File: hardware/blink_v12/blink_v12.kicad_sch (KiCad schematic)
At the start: 178 parts, among them J1 Conn_01x02, J14 Conn_02x16_Odd_Even, J15 Conn_01x01, J16 Conn_01x01, J5 Conn_01x06_Pin, J6 Conn_01x03, J7 Conn_01x06_Pin, J9 USB_C_Receptacle, Q1 AO3400A, Q2 AO3400A, Q3 2N7002, Q4 2N7002, Q5 2N7002, SW1 SW_SPDT, SW2 SW_Push_4PDT, SW3 SW_Push_4PDT, SW4 SW_Push_4PDT, U1 AMS1117-3.3, U10 TMP112AIDRLR, U11 MAX40200AUK, U12 MAX40200AUK, U13 AMS1117-3.3, U14 SN74LVC1G14DBV, U15 BQ29702DSER, U16 TPS63060, U3 M24C02-RMN, U4 STM32F405RGTx, U5 SN74LVC1G14DBV, U6 SN74LVC1G14DBV, U7 CH340C, U8 USBLC6-2P6, U9 MCP73832-2-OT, X1 GTXO-14V (2.048MHz), Y1 16MHz

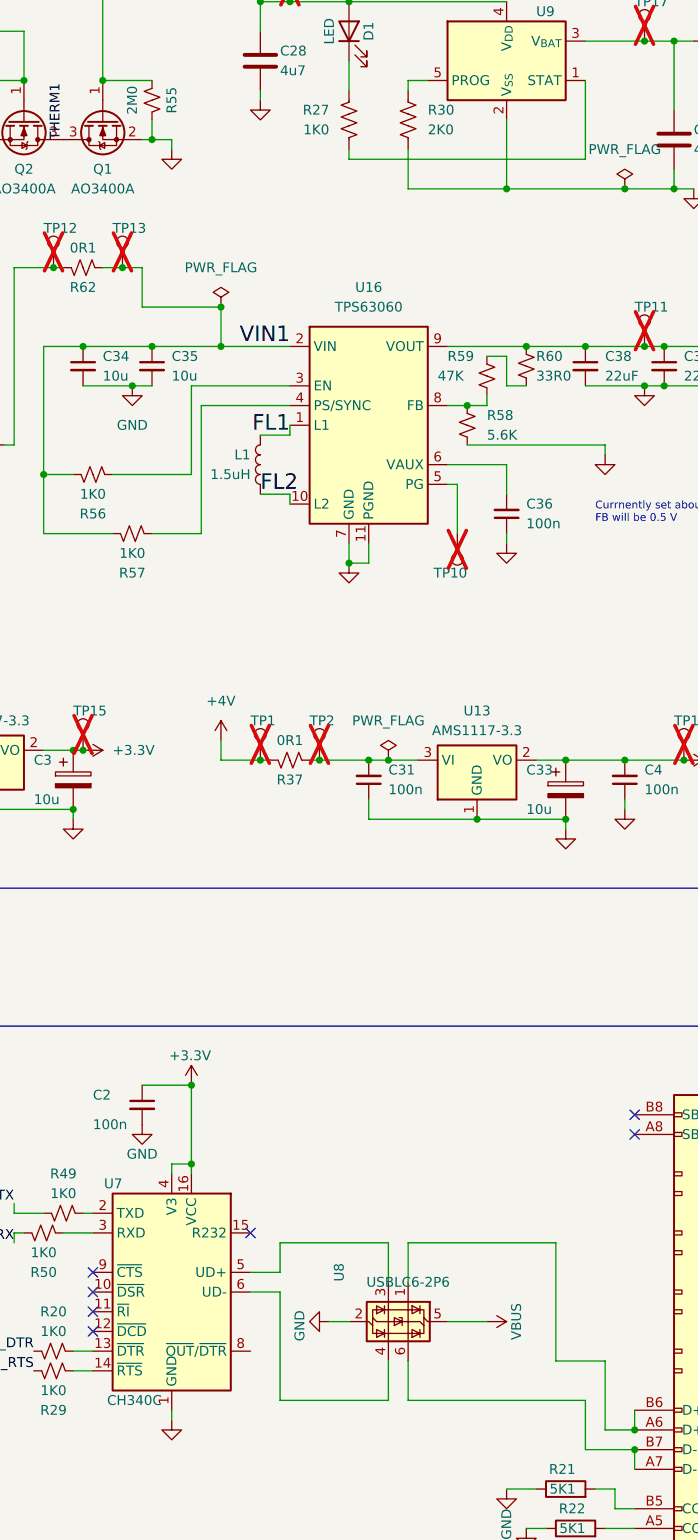
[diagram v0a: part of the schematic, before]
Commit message: fix symbol for USBLC6-2P6 that seems chaged in kicad 8
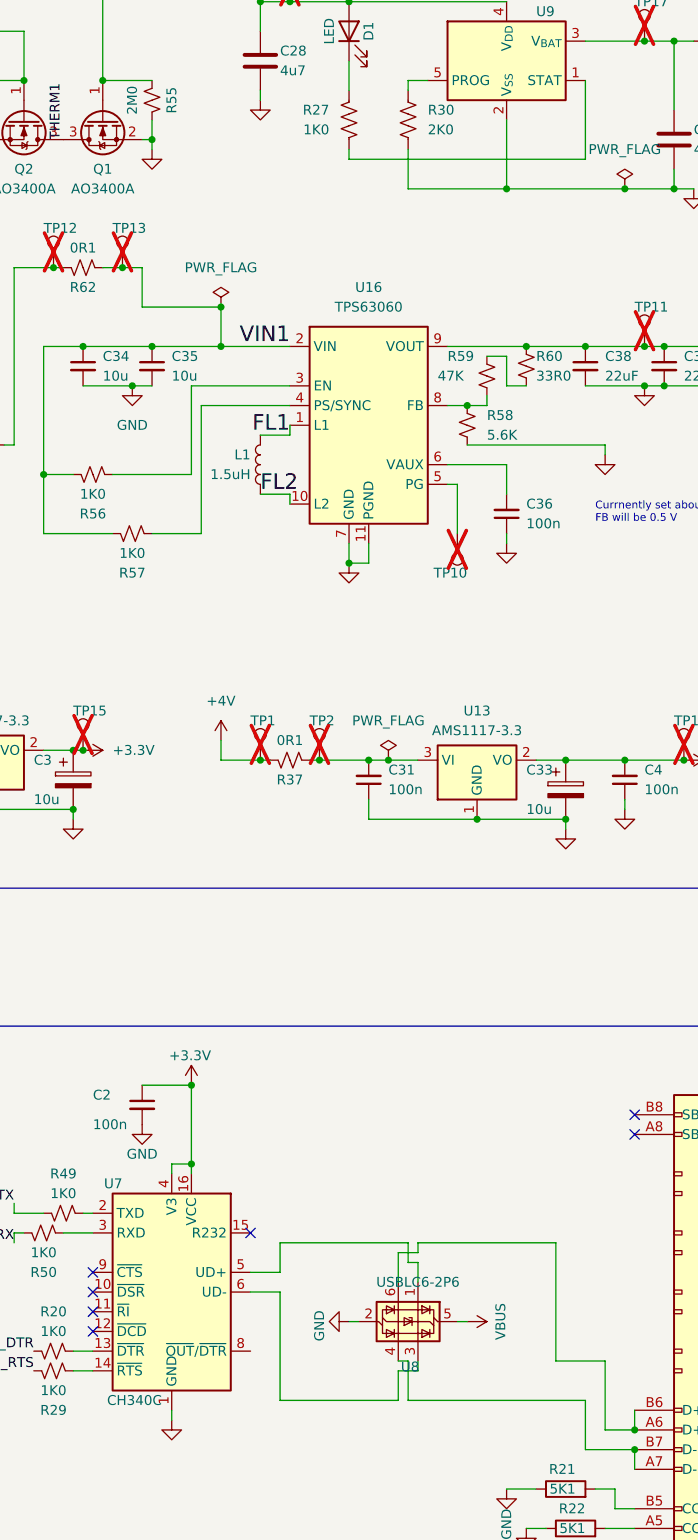
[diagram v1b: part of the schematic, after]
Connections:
- net at U7.5 (UD+): now also U8.1 (I/O1); no longer U8.3 (I/O2)
- net at U7.6 (UD-): now also U8.3 (I/O1); no longer U8.4 (I/O2)
- net at J9.A6 (D+), J9.B6 (D+): now also U8.6 (I/O2); no longer U8.1 (I/O1)
- net at J9.A7 (D-), J9.B7 (D-): now also U8.4 (I/O2); no longer U8.6 (I/O1)
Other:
- moved on the sheet: U8

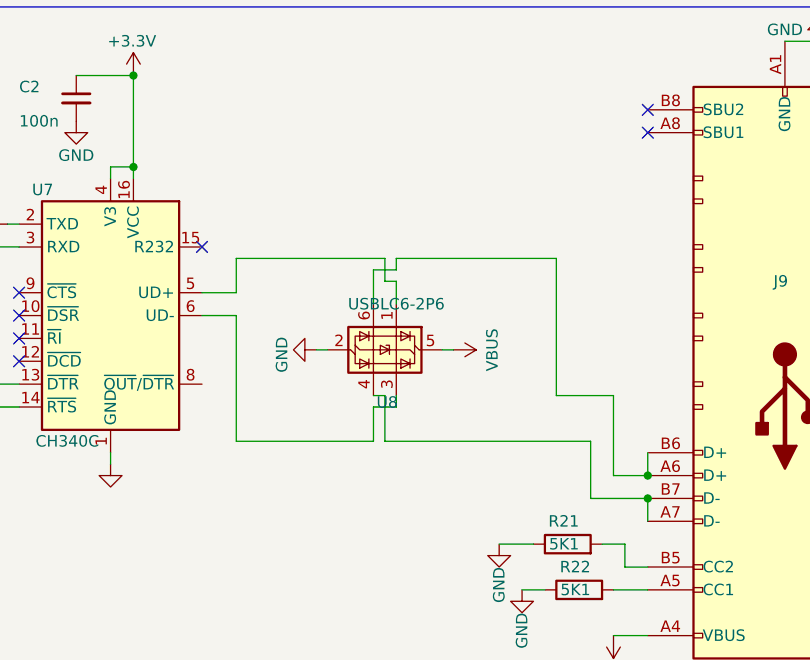
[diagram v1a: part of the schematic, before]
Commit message: fix up schematic for new USBLC6-2P6  footprint
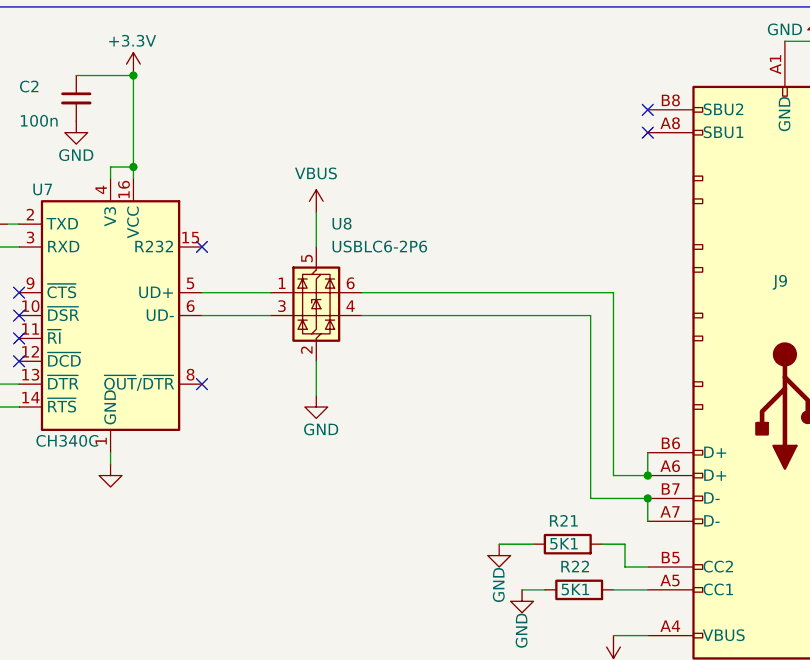
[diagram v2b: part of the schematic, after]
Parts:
- U8: JLCPCB Part # C2827693 -> (none); JLCPCB Rotation Offset 270 -> (none)
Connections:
- no-connect marks 42 -> 43

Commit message: remove the battery protection circuit
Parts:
- removed C37: 100n, Capacitor_SMD:C_0402_1005Metric, symbol Device:C_Small
- removed Q1, Q2: AO3400A, Package_TO_SOT_SMD:SOT-23, symbol Transistor_FET:AO3400A
- removed R14: 330R, Resistor_SMD:R_0603_1608Metric, symbol Device:R_Small_US
- removed R18: 2K2, Resistor_SMD:R_0603_1608Metric, symbol Device:R_Small_US
- removed R34, R55: 2M0, Resistor_SMD:R_0603_1608Metric, symbol Device:R_Small_US
- removed U15: BQ29702DSER, Package_SON:WSON-6_1.5x1.5mm_P0.5mm, symbol Battery_Management:BQ297xy
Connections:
- net GND: now also J1.1 (Pin_1), TP21.1

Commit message: moved the test points off rails
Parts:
- removed TP21, TP6, TP7, TP8: ~, TestPoint:TestPoint_THTPad_D1.5mm_Drill0.7mm, symbol Connector:TestPoint

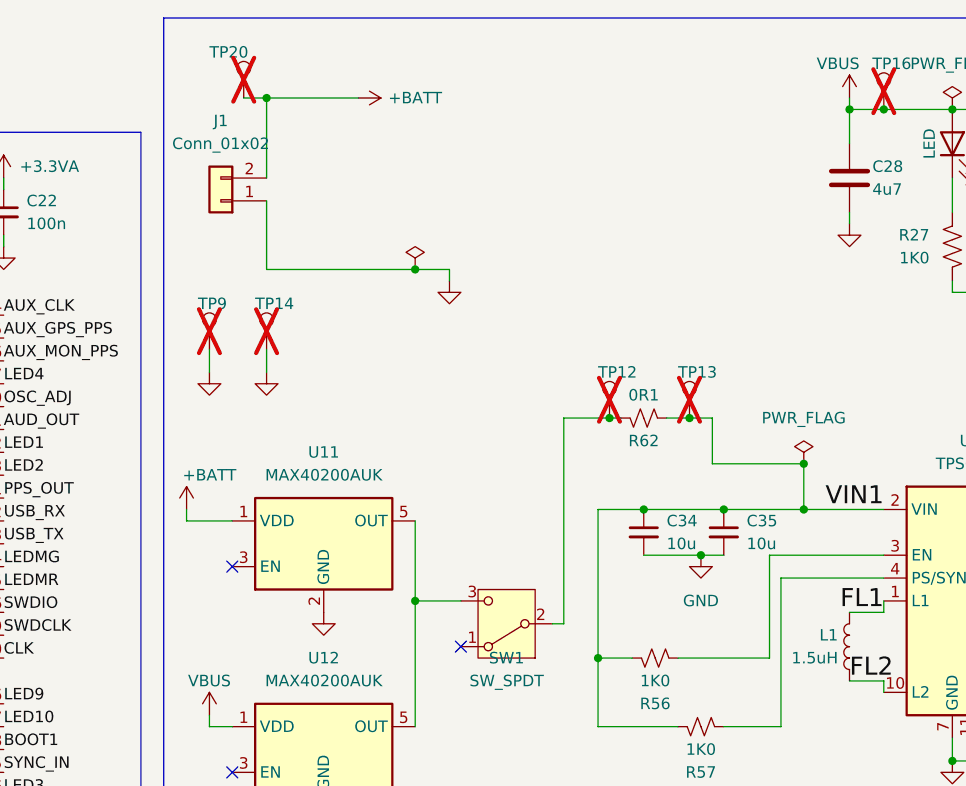
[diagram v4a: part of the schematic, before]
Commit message: fix rotations for V12 blink
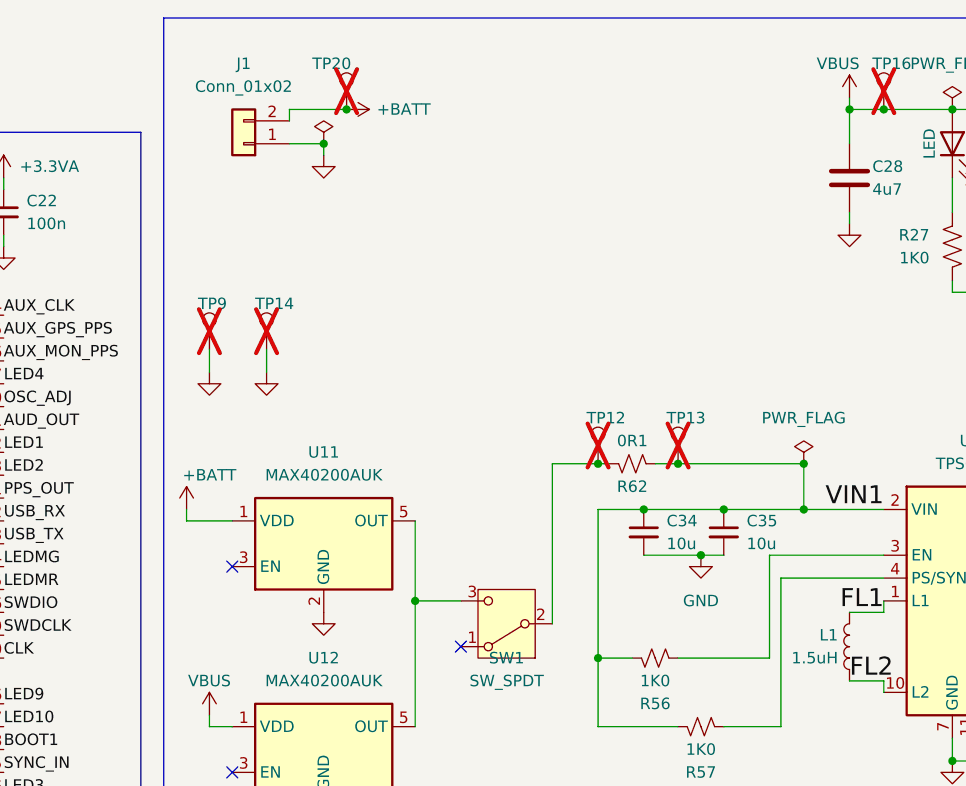
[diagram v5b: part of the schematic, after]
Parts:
- D4: JLCPCB Position Offset 0,-0.75 -> 0,0
- J1: JLCPCB Rotation Offset (none) -> 180
- J6, Q3, Q4, Q5, U1, U13: JLCPCB Rotation Offset 180 -> 0
- SW1: JLCPCB Position Offset 3.9,-1.2 -> 0,0
- U10: JLCPCB Rotation Offset 270 -> 180
- U11, U12, U9: JLCPCB Rotation Offset 270 -> 90
- U3, U4, U7: JLCPCB Rotation Offset 270 -> 0
- U8: JLCPCB Rotation Offset (none) -> 270
- U? (x3): JLCPCB Rotation Offset (none) -> 90
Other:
- moved on the sheet: J1, R62, TP12, TP13, TP20

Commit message: add 3D model for USB connector
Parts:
- J9: footprint Connector_USB:USB_C_Receptacle_HRO_TYPE-C-31-M-12 -> blinky_footprints:USB_C_Receptacle_HRO_TYPE-C-31-M-12
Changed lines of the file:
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@@
 			)
 		)
-		(property "Footprint" "Connector_USB:USB_C_Receptacle_HRO_TYPE-C-31-M-12"
+		(property "Footprint" "blinky_footprints:USB_C_Receptacle_HRO_TYPE-C-31-M-12"
 			(at 401.32 199.39 0)
 			(effects
@@
 			(at 405.13 199.39 0)
 			(effects
-				(font
-					(size 1.27 1.27)
-				)
-				(hide yes)
-			)
-		)
-		(property "JLCPCB#" ""
-			(at 405.13 199.39 0)
-			(effects

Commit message: fixed offset for JLCPCB
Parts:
- C?: JLCPCB Rotation Offset (none) -> 180
- D4: JLCPCB Position Offset 0,0 -> 0,0.7
- J9: JLCPCB Position Offset 0,1.1 -> 0,1.5
- J? (x4): JLCPCB Position Offset (none) -> 0,-13.0
- SW1: JLCPCB Position Offset 0,0 -> 0.1,4.1
- SW2, SW3, SW4: JLCPCB Position Offset -1.35,-6.38 -> 0,-6.7
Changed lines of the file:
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@@
 			)
 		)
-		(property "JLCPCB Position Offset" "0,0"
+		(property "JLCPCB Position Offset" "0.1,4.1"
 			(at 303.53 80.01 0)
 			(effects
@@
 			)
 		)
-		(property "JLCPCB Position Offset" "-1.35,-6.38"
+		(property "JLCPCB Position Offset" "0,-6.7"
 			(at 283.21 161.29 0)
 			(effects
@@
 			)
 		)
+		(property "JLCPCB Position Offset" "0,-13.0"
+			(at 237.49 251.46 0)
+			(effects
+				(font
+					(size 1.27 1.27)
+				)
+				(hide yes)
+			)
+		)
 		(pin "1"
 		)
@@
 			)
 		)
+		(property "JLCPCB Position Offset" "0,-13.0"
+			(at 137.16 233.68 0)
+			(effects
+				(font
+					(size 1.27 1.27)
+				)
+				(hide yes)
+			)
+		)
 		(pin "1"
 		)
@@
 			)
 		)
-		(property "JLCPCB Position Offset" "-1.35,-6.38"
+		(property "JLCPCB Position Offset" "0,-6.7"
 			(at 234.95 162.56 0)
 			(effects
@@
 			)
 		)
+		(property "JLCPCB Position Offset" "0,-13.0"
+			(at 127 208.28 0)
+			(effects
+				(font
+					(size 1.27 1.27)
+				)
+				(hide yes)
+			)
+		)
 		(pin "1"
 		)
@@
 			)
 		)
-		(property "JLCPCB Position Offset" "-1.35,-6.38"
+		(property "JLCPCB Position Offset" "0,-6.7"
 			(at 260.35 161.29 0)
 			(effects
@@
 			)
 		)
-		(property "JLCPCB Position Offset" "0,0"
+		(property "JLCPCB Position Offset" "0,0.7"
 			(at 123.19 135.89 0)
 			(effects
@@
 			)
 		)
+		(property "JLCPCB Rotation Offset" "180"
+			(at 63.5 259.08 0)
+			(effects
+				(font
+					(size 1.27 1.27)
+				)
+				(hide yes)
+			)
+		)
 		(pin "1"
 		)
@@
 			)
 		)
-		(property "JLCPCB Position Offset" "0,1.1"
+		(property "JLCPCB Position Offset" "0,1.5"
 			(at 405.13 199.39 0)
 			(effects
@@
 			(at 288.29 218.44 0)
 			(effects
+				(font
+					(size 1.27 1.27)
+				)
+				(hide yes)
+			)
+		)
+		(property "JLCPCB Position Offset" "0,-13.0"
+			(at 288.29 218.44 0)
+			(effects
